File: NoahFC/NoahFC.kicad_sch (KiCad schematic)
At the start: 25 parts, among them J1 CH1, J10 GND, J2 CH2, J3 MPU6050, J4 FTDI, J5 VCC, J6 CH3, J7 PPM, J8 GPS, J9 CH4, U1 ATmega328-A, U3 AMS1117-5.0, Y1 16Mhz

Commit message: revision 1
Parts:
- added J11: SCK, TestPoint:TestPoint_Pad_1.0x1.0mm, symbol Connector:Conn_01x01_Female
- added J12: MISO, TestPoint:TestPoint_Pad_1.0x1.0mm, symbol Connector:Conn_01x01_Female
- added J13: VCC, TestPoint:TestPoint_Pad_4.0x4.0mm, symbol Connector:Conn_01x01_Female
- added J14: GND, TestPoint:TestPoint_Pad_4.0x4.0mm, symbol Connector:Conn_01x01_Female
- added R5: 100K, Resistor_SMD:R_0805_2012Metric, symbol Device:R
- added R6: 10K, Resistor_SMD:R_0805_2012Metric, symbol Device:R
- C3: value 100nF -> 1nF
- C5: value 100uF -> 10uF
- D1: value PWR -> GPS; footprint LED_SMD:LED_0603_1608Metric -> LED_SMD:LED_0805_2012Metric
- D2: value GPS -> MODE; footprint LED_SMD:LED_0603_1608Metric -> LED_SMD:LED_0805_2012Metric
- D3: value MODE -> PWR; footprint LED_SMD:LED_0603_1608Metric -> LED_SMD:LED_0805_2012Metric
- U1: value ATmega328-A -> ATmega328
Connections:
- net 5V: no longer C3.1, J1.2 (Pin_2), J2.2 (Pin_2), J7.2 (Pin_2), J9.2 (Pin_2)
- net GND: now also J14.1 (Pin_1), R6.2
- net GPS_RX: now also U1.32 (PD2); no longer U1.11 (PD7)
- net VCC: now also J13.1 (Pin_1), R5.1
- net XTAL1: now reaches C1.1, U1.7 (XTAL1/PB6), Y1.2
- net LED_GPS: now reaches R2.1
- net LED_GPS: now also U1.9 (PD5); no longer U1.32 (PD2)
- net MISO: now reaches U1.16 (PB4)
- net MISO: now also J12.1 (Pin_1)
- net SCK: now reaches U1.17 (PB5)
- net SCK: now also J11.1 (Pin_1)
- net ADC6: now reaches U1.19 (ADC6)
- net LED_MODE: now reaches R3.1, U1.2 (PD4)
- net ADC7: now reaches U1.22 (ADC7)
- net A0: now reaches U1.23 (PC0)
- net A1: now reaches U1.24 (PC1)
- net VOLTAGE_READ: now reaches U1.25 (PC2)
- net VOLTAGE_READ: now also R5.2, R6.1
- net A3: now reaches U1.26 (PC3)
- net RESET: now reaches R1.1, U1.29 (~{RESET}/PC6)
- net RESET: now also C3.1
- net XTAL2: now reaches C2.1, U1.8 (XTAL2/PB7), Y1.1
- net LED_PWR: now reaches R4.1
- net LED_PWR: now also U1.11 (PD7); no longer U1.9 (PD5)
- net 5V_BEC: now reaches J6.2 (Pin_2)
- net 5V_BEC: now also J1.2 (Pin_2), J2.2 (Pin_2), J7.2 (Pin_2), J9.2 (Pin_2)
- no-connect marks 13 -> 4

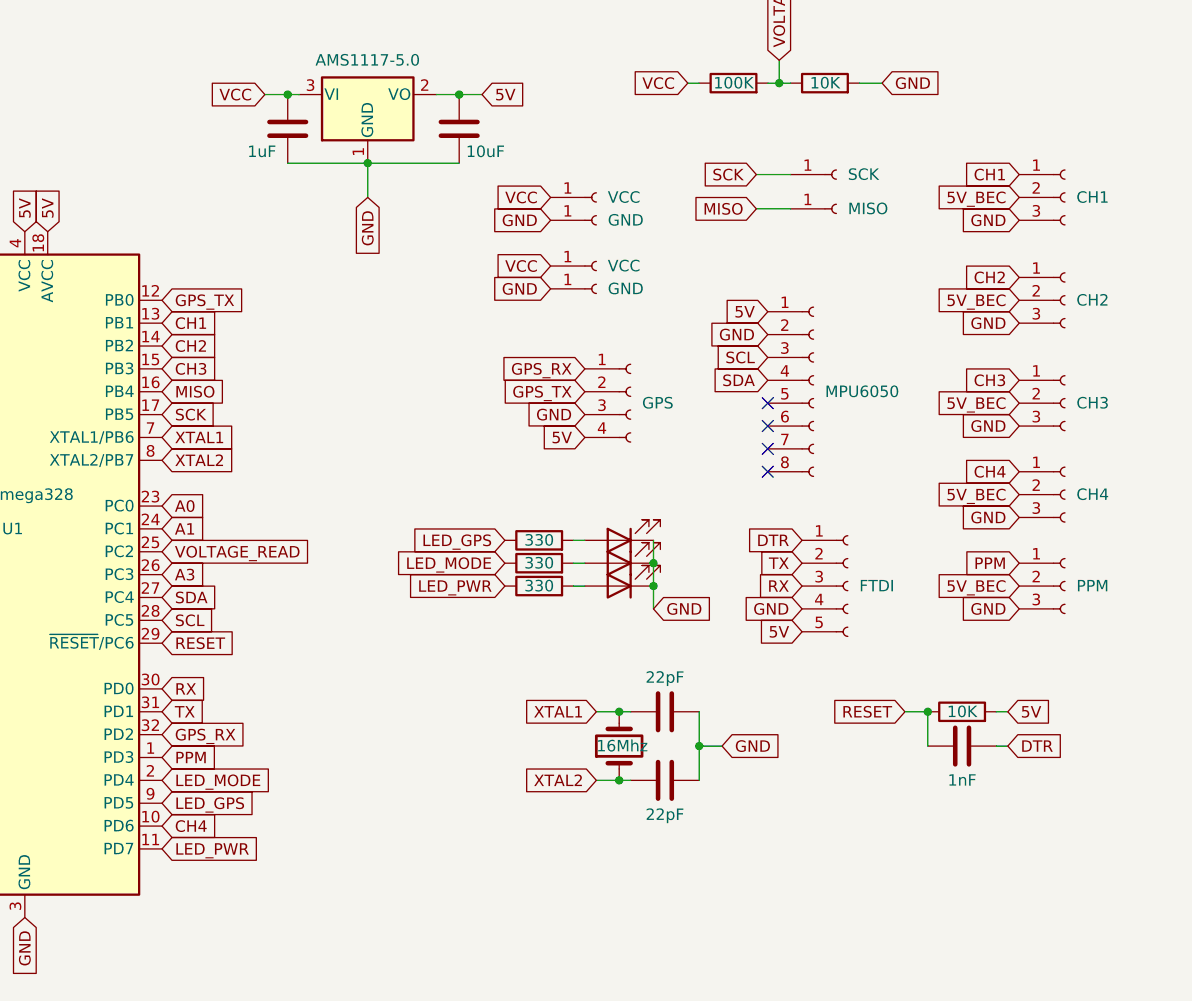
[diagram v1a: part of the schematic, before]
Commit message: remove one aleron servo
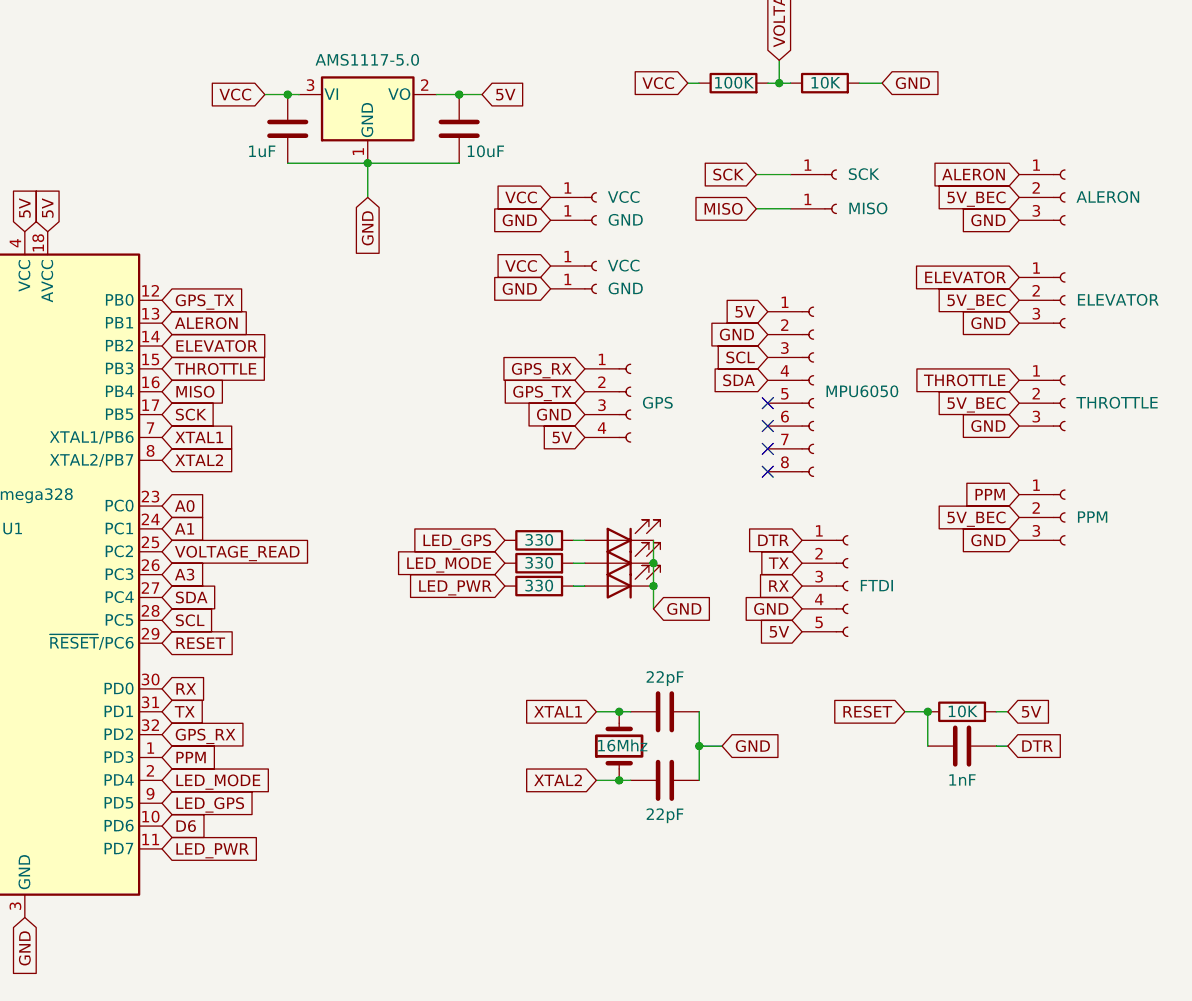
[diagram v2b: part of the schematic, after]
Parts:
- removed J9: CH4, Connector_PinHeader_2.54mm:PinHeader_1x03_P2.54mm_Vertical, symbol Connector:Conn_01x03_Female
- J1: value CH1 -> ALERON
- J2: value CH2 -> ELEVATOR
- J6: value CH3 -> THROTTLE
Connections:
- net CH1 renamed ALERON
- net CH2 renamed ELEVATOR
- net CH3 renamed THROTTLE
- net CH4 renamed D6

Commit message: route board
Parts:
- added J15: A1, TestPoint:TestPoint_Pad_1.0x1.0mm, symbol Connector:Conn_01x01_Female
- added J16: A3, TestPoint:TestPoint_Pad_1.0x1.0mm, symbol Connector:Conn_01x01_Female
- added J17: D6, TestPoint:TestPoint_Pad_1.0x1.0mm, symbol Connector:Conn_01x01_Female
- added J9: A0, TestPoint:TestPoint_Pad_1.0x1.0mm, symbol Connector:Conn_01x01_Female
- J1: value ALERON -> ALE
- J2: value ELEVATOR -> ELE
- J6: value THROTTLE -> THR
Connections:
- net A0: now also J9.1 (Pin_1)
- net A1: now also J15.1 (Pin_1)
- net A3: now also J16.1 (Pin_1)
- net D6: now also J17.1 (Pin_1)
- net GND: no longer J1.3 (Pin_3), J2.3 (Pin_3), J6.3 (Pin_3), J7.3 (Pin_3)
- new net GND_BEC: J1.3 (Pin_3), J2.3 (Pin_3), J6.3 (Pin_3), J7.3 (Pin_3)

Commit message: pin improve
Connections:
- net 5V: now also J7.2 (Pin_2)
- net 5V_BEC: no longer J7.2 (Pin_2)
- net GND: now also J7.3 (Pin_3)
- net GND_BEC: no longer J7.3 (Pin_3)
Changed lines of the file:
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@@
     )
   )
-  (global_label "5V_BEC" (shape input) (at 222.25 124.46 180) (fields_autoplaced)
+  (global_label "5V" (shape input) (at 222.25 124.46 180) (fields_autoplaced)
     (effects (font (size 1.27 1.27)) (justify right))
-    (property "Intersheet References" "${INTERSHEET_REFS}" (id 0) (at 212.8821 124.3806 0)
+    (property "Intersheet References" "${INTERSHEET_REFS}" (id 0) (at 217.5388 124.3806 0)
       (effects (font (size 1.27 1.27)) (justify right) hide)
     )
@@
     )
   )
-  (global_label "GND_BEC" (shape input) (at 222.25 127 180) (fields_autoplaced)
+  (global_label "GND" (shape input) (at 222.25 127 180) (fields_autoplaced)
     (effects (font (size 1.27 1.27)) (justify right))
-    (property "Intersheet References" "${INTERSHEET_REFS}" (id 0) (at 211.3098 126.9206 0)
+    (property "Intersheet References" "${INTERSHEET_REFS}" (id 0) (at 215.9664 126.9206 0)
       (effects (font (size 1.27 1.27)) (justify right) hide)
     )

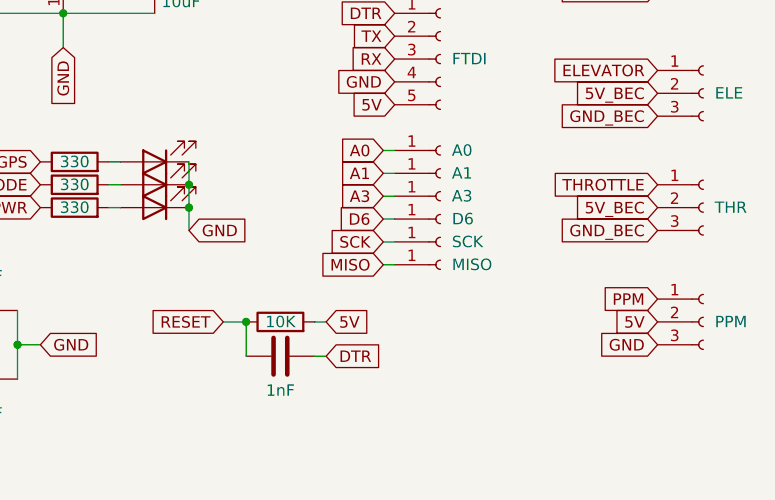
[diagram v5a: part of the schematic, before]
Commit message: add RESET pad
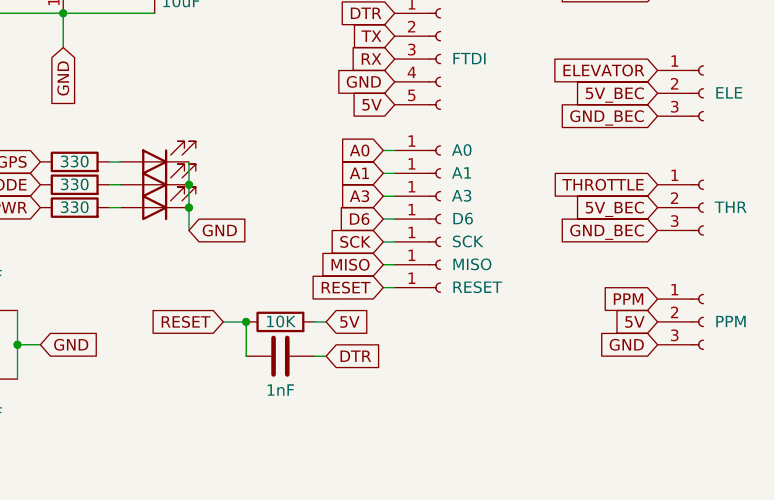
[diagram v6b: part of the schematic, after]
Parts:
- added J18: RESET, TestPoint:TestPoint_Pad_1.0x1.0mm, symbol Connector:Conn_01x01_Female
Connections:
- net RESET: now also J18.1 (Pin_1)
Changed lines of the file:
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@@
+    (stroke (width 0) (type default) (color 0 0 0 0))
+  )
+  (wire (pts (xy 191.77 120.65) (xy 193.04 120.65))
     (stroke (width 0) (type default) (color 0 0 0 0))
   )
@@
     (effects (font (size 1.27 1.27)) (justify right))
     (property "Intersheet References" "${INTERSHEET_REFS}" (id 0) (at 215.9664 126.9206 0)
+      (effects (font (size 1.27 1.27)) (justify right) hide)
+    )
+  )
+  (global_label "RESET" (shape input) (at 191.77 120.65 180) (fields_autoplaced)
+    (effects (font (size 1.27 1.27)) (justify right))
+    (property "Intersheet References" "${INTERSHEET_REFS}" (id 0) (at 183.6117 120.5706 0)
       (effects (font (size 1.27 1.27)) (justify right) hide)
     )
@@
     (pin "1")
   )
+  (symbol (lib_id "Connector:Conn_01x01_Female") (at 198.12 120.65 0) (unit 1)
+    (in_bom yes) (on_board yes) (fields_autoplaced)
+    (property "Reference" "J18" (id 0) (at 199.39 119.3799 0)
+      (effects (font (size 1.27 1.27)) (justify left) hide)
+    )
+    (property "Value" "RESET" (id 1) (at 199.39 120.6499 0)
+      (effects (font (size 1.27 1.27)) (justify left))
+    )
+    (property "Footprint" "TestPoint:TestPoint_Pad_1.0x1.0mm" (id 2) (at 198.12 120.65 0)
+      (effects (font (size 1.27 1.27)) hide)
+    )
+    (property "Datasheet" "~" (id 3) (at 198.12 120.65 0)
+      (effects (font (size 1.27 1.27)) hide)
+    )
+    (pin "1")
+  )
   (symbol (lib_id "Connector:Conn_01x01_Female") (at 198.12 113.03 0) (unit 1)
     (in_bom yes) (on_board yes) (fields_autoplaced)
@@
       (reference "J17") (unit 1) (value "D6") (footprint "TestPoint:TestPoint_Pad_1.0x1.0mm")
     )
+    (path "/a1f0cfc9-23af-4faa-86fe-1abc768ffe93"
+      (reference "J18") (unit 1) (value "RESET") (footprint "TestPoint:TestPoint_Pad_1.0x1.0mm")
+    )
     (path "/85cd2359-33a4-4487-905a-7b387e0f6b66"

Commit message: add rev2 version board
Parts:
- removed J15: A1, TestPoint:TestPoint_Pad_1.0x1.0mm, symbol Connector:Conn_01x01_Female
- removed J16: A3, TestPoint:TestPoint_Pad_1.0x1.0mm, symbol Connector:Conn_01x01_Female
- removed J17: D6, TestPoint:TestPoint_Pad_1.0x1.0mm, symbol Connector:Conn_01x01_Female
- removed J3: MPU6050, Connector_PinHeader_2.54mm:PinHeader_1x08_P2.54mm_Vertical, symbol Connector:Conn_01x08_Female
- removed J9: A0, TestPoint:TestPoint_Pad_1.0x1.0mm, symbol Connector:Conn_01x01_Female
- added C10: 10uF, Capacitor_SMD:C_0805_2012Metric, symbol Device:C
- added C11: 22uF, Capacitor_SMD:C_0805_2012Metric, symbol Device:C
- added C12, C13: 22pF, Capacitor_SMD:C_0805_2012Metric, symbol Device:C
- added C17, C7, C8: 100nF, Capacitor_SMD:C_0805_2012Metric, symbol Device:C
- added C18, C19: 47uF, Capacitor_Tantalum_SMD:CP_EIA-3216-18_Kemet-A, symbol Device:C_Polarized
- added C20: 4.7uF, Capacitor_SMD:C_0805_2012Metric, symbol Device:C
- added C21: 220nF, Capacitor_SMD:C_0805_2012Metric, symbol Device:C
- added C6: 10nF, Capacitor_SMD:C_0805_2012Metric, symbol Device:C
- added C9: 2200pF, Capacitor_SMD:C_0805_2012Metric, symbol Device:C
- added J16: CAM, Connector_PinHeader_2.54mm:PinHeader_1x02_P2.54mm_Vertical, symbol Connector:Conn_01x02_Male
- added J17: VTX, Connector_PinHeader_2.54mm:PinHeader_1x02_P2.54mm_Vertical, symbol Connector:Conn_01x02_Male
- added R10, R9: 75, Resistor_SMD:R_0805_2012Metric, symbol Device:R
- added R7, R8: 10K, Resistor_SMD:R_0805_2012Metric, symbol Device:R
- added U2: MPU-6050, Sensor_Motion:InvenSense_QFN-24_4x4mm_P0.5mm, symbol Sensor_Motion:MPU-6050
- added U4: AMS1117-3.3, Package_TO_SOT_SMD:SOT-223-3_TabPin2, symbol Regulator_Linear:AP1117-33
- added U5: MAX7456EUI+, SOP65P637X110-28N, symbol MAX7456EUI_:MAX7456EUI+
- added U6: HMC5883L, LPCC-16, symbol HMC5883L:HMC5883L
- added Y2: 27Mhz, Crystal:Crystal_SMD_3225-4Pin_3.2x2.5mm, symbol Device:Crystal
- Y1: footprint Crystal:Crystal_SMD_HC49-SD -> Crystal:Crystal_SMD_3225-4Pin_3.2x2.5mm
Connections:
- net D6 is gone; now on net ELEVATOR: U1.10 (PD6)
- net 5V: now also R4.1, C10.2, U4.3 (VI), U5.21 (AVDD), U5.24 (PVDD), U5.3 (DVDD)
- net ELEVATOR: no longer U1.14 (PB2)
- net GND: now also C10.1, C11.1, C12.2, C13.2, C20.1, C6.1, C7.2, C8.2, C9.2, J16.1 (Pin_1), J17.1 (Pin_1), R9.2, U2.1 (CLKIN), U2.11 (FSYNC), U2.18 (GND), U4.1 (GND), U5.20 (AGND), U5.23 (PGND), U5.4 (DGND), U6.11 (GND@2), U6.9 (GND@1)
- net LED_GPS: now also U1.11 (PD7); no longer U1.9 (PD5)
- net MISO: now also U5.11 (SDOUT)
- net SCK: now also U5.10 (SCLK)
- net SCL: now also R7.2, U2.23 (SCL), U6.1 (SCL)
- net SDA: now also R8.2, U2.24 (SDA), U6.16 (SDA)
- net THROTTLE: now also U1.9 (PD5); no longer U1.15 (PB3)
- net A0: no longer names the net of U1.23 (PC0)
- net A1: no longer names the net of U1.24 (PC1)
- net A3: no longer names the net of U1.26 (PC3)
- net ADC6: no longer names the net of U1.19 (ADC6)
- net ADC7: no longer names the net of U1.22 (ADC7)
- removed net LED_PWR: R4.1, U1.11 (PD7)
- new net: C8.1, U2.10 (REGOUT)
- new net: C9.1, U2.20 (CPOUT)
- new net: C21.1, U6.8 (SETP)
- new net: C21.2, U6.12 (SETC)
- new net: C17.2, J16.2 (Pin_2), R9.1
- new net: C19.1, U5.26 (VOUT)
- new net: C18.2, C19.2, R10.1
- new net: C17.1, U5.22 (VIN)
- new net: J17.2 (Pin_2), R10.2
- new net: C20.2, U6.10 (C1)
- new net: C18.1, U5.25 (SAG)
- new net 3.3V: C11.2, C6.2, C7.1, R7.1, R8.1, U2.13 (VDD), U2.8 (VDDIO), U4.2 (VO), U6.13 (VDDIO), U6.2 (VDD), U6.4 (S1)
- new net MOSI: U1.15 (PB3), U5.9 (SDIN)
- new net SS: U1.14 (PB2), U5.8 (~{CS})
- new net XTAL1_OSD: C12.1, U5.6 (XFB), Y2.1
- new net XTAL2_OSD: C13.1, U5.5 (CLKIN), Y2.2
- no-connect marks 4 -> 21
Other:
- moved on the sheet: U1

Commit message: update scheme / design and board
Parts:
- removed C1, C12, C13, C2: 22pF, Capacitor_SMD:C_0805_2012Metric, symbol Device:C
- removed J16: CAM, Connector_PinHeader_2.54mm:PinHeader_1x02_P2.54mm_Vertical, symbol Connector:Conn_01x02_Male
- added J3: CAM, Connector_PinHeader_2.54mm:PinHeader_1x03_P2.54mm_Vertical, symbol Connector:Conn_01x03_Male
- C9: value 2200pF -> 2.2nF
- J17: footprint Connector_PinHeader_2.54mm:PinHeader_1x02_P2.54mm_Vertical -> Connector_PinHeader_2.54mm:PinHeader_1x03_P2.54mm_Vertical; symbol Connector:Conn_01x02_Male -> Connector:Conn_01x03_Male
- Y1: footprint Crystal:Crystal_SMD_3225-4Pin_3.2x2.5mm -> Crystal:Resonator_SMD_Murata_CSTxExxV-3Pin_3.0x1.1mm; symbol Device:Crystal -> Device:Resonator
- Y2: symbol Device:Crystal -> Device:Resonator
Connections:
- net 5V: no longer J7.2 (Pin_2)
- net 5V_BEC: now also J7.2 (Pin_2)
- net ALERON: now also J1.3 (Pin_3); no longer J1.1 (Pin_1)
- net ELEVATOR: now also J2.3 (Pin_3); no longer J2.1 (Pin_1)
- net GND: now also Y1.2, Y2.2, J3.1 (Pin_1); no longer J7.3 (Pin_3)
- net GND_BEC: now also J1.1 (Pin_1), J2.1 (Pin_1), J6.1 (Pin_1), J7.1 (Pin_1); no longer J1.3 (Pin_3), J2.3 (Pin_3), J6.3 (Pin_3)
- net PPM: now also J7.3 (Pin_3); no longer J7.1 (Pin_1)
- net THROTTLE: now also J6.3 (Pin_3); no longer J6.1 (Pin_1)
- net XTAL1: now also Y1.3; no longer Y1.2
- net XTAL2_OSD: now also Y2.3; no longer Y2.2
- net at C17.2, R9.1: now also J3.3 (Pin_3)
- net at J17.2 (Pin_2): no longer R10.2
- new net: J17.3 (Pin_3), R10.2
- no-connect marks 21 -> 23
